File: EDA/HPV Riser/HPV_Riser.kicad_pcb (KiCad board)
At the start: 2 copper layers, 200 x 47 mm, 6 parts, among them J1 PowerMac_PDS, J2 PowerMac_PDS

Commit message: HPV PCB routing session
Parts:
- added G***: LOGO, Connector_Apple:Apple_Logo, F.Cu at (241.3, 85.7)
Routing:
- net GND: track 0.00 -> 688.4 mm, vias 0 -> 15
- net +5V: track 0.00 -> 550.9 mm, vias 0 -> 21
- net /A25: track 0.00 -> 177.6 mm, vias 0 -> 4
- net /A31: track 0.00 -> 127.8 mm, vias 0 -> 4
- net /D41: track 0.00 -> 115.8 mm, vias 0 -> 4
- net /D40: track 0.00 -> 114.3 mm, vias 0 -> 4
- net /D43: track 0.00 -> 98.1 mm, vias 0 -> 2
- net /DataRtry: track 0.00 -> 96.2 mm, vias 0 -> 4
- net /D60: track 0.00 -> 86.0 mm, vias 0 -> 6
- net /NuDump: track 0.00 -> 84.2 mm, vias 0 -> 4
- net /D37: track 0.00 -> 80.3 mm, vias 0 -> 2
- net /D59: track 0.00 -> 76.3 mm, vias 0 -> 2
- net /D35: track 0.00 -> 71.3 mm, vias 0 -> 2
- net +12V: track 0.00 -> 71.1 mm, vias 0 -> 3
- net /D62: track 0.00 -> 70.3 mm, vias 0 -> 4
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- added copper zone on B.Cu, net GND
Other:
- net class Default: clearance 0.254 -> 0.1778
- net class GND: clearance 0.254 -> 0.1778
- rule trace_clearance: 0.254 -> 0.1778
- board text added: "PowerMac 6100 HPV Riser REV 1.0 Michel "demik" Depeige 68kmla JLCJLCJLCJLC"
- board text removed: "PowerMac 6100 HPV Riser REV 1.0 Michel "demik" Depeige 68kmla"

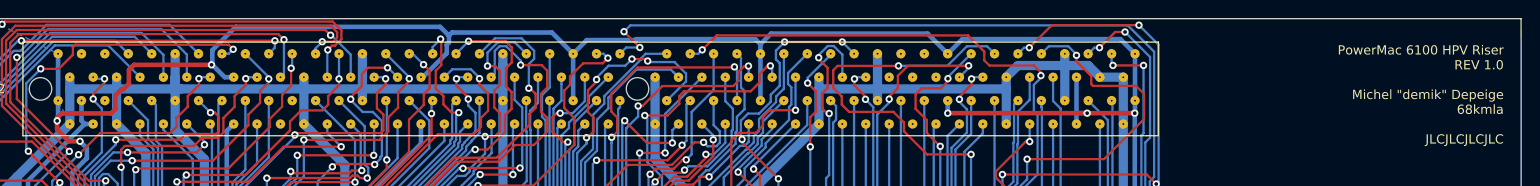
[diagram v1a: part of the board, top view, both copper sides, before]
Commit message: increased EDAC_302-182-520-900 holes from 0.2 to 0.6
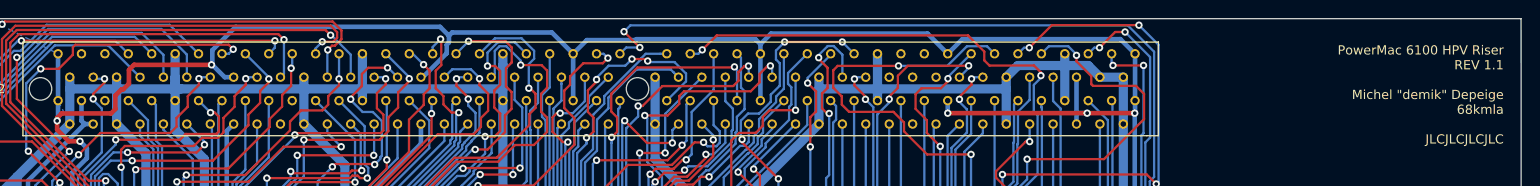
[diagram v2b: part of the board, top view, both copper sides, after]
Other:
- board text added: "PowerMac 6100 HPV Riser REV 1.1 Michel "demik" Depeige 68kmla JLCJLCJLCJLC"
- board text removed: "PowerMac 6100 HPV Riser REV 1.0 Michel "demik" Depeige 68kmla JLCJLCJLCJLC"

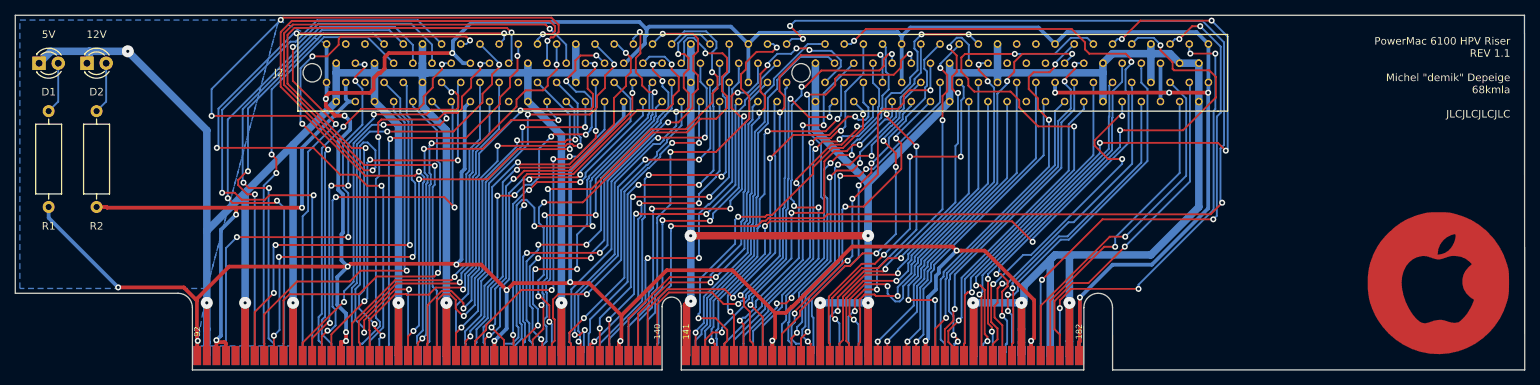
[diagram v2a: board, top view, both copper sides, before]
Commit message: HPV Riser Rev 1.2: Routing and PCB Edge fixes
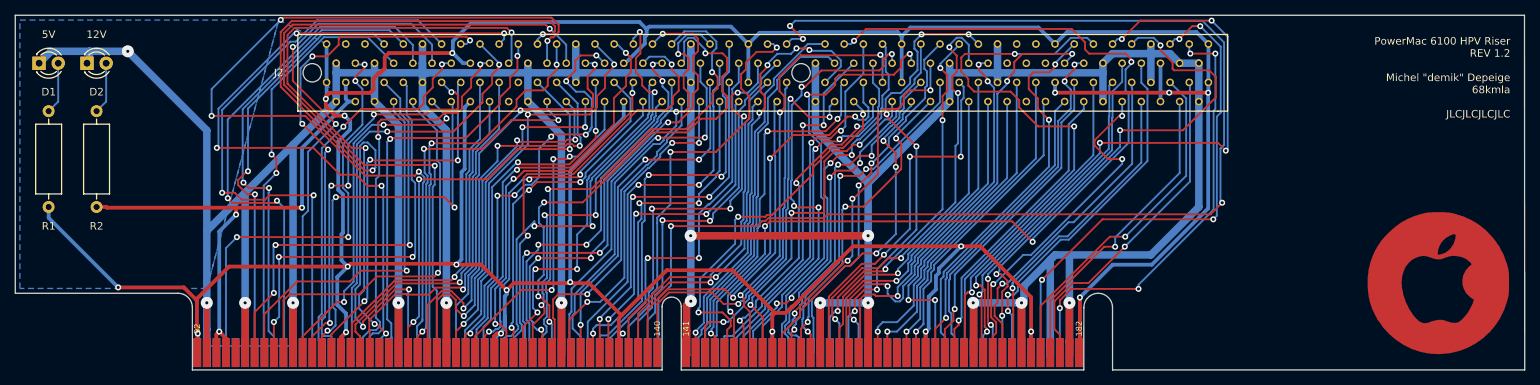
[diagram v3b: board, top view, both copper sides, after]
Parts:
- moved J1 0.38 mm to (135.3, 95.5)
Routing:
- net +5V: track 550.9 -> 559.0 mm, vias 21 -> 20
- net /XferStart: track 54.2 -> 58.3 mm
- net +12V: track 71.1 -> 74.6 mm
- net /XferAck: track 67.8 -> 64.4 mm
- net /NuDump: track 84.2 -> 86.5 mm
- net /A11: track 58.0 -> 55.7 mm, vias 4 -> 2
- net /A17: track 49.9 -> 47.7 mm
- net /DataRtry: track 96.2 -> 98.2 mm
- net /D4: track 47.7 -> 49.6 mm
- net /D13: track 47.8 -> 49.7 mm
- net /A2: track 45.3 -> 47.2 mm
- net /TS1: track 45.7 -> 47.5 mm
- net /AddrRtry: track 52.6 -> 54.4 mm
- net /CacheIn: track 47.5 -> 49.2 mm
- net /D39: track 66.7 -> 68.5 mm
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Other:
- net class +5V: clearance 0.254 -> 0.1778
- board text added: "PowerMac 6100 HPV Riser REV 1.2 Michel "demik" Depeige 68kmla JLCJLCJLCJLC"
- board text removed: "PowerMac 6100 HPV Riser REV 1.1 Michel "demik" Depeige 68kmla JLCJLCJLCJLC"
